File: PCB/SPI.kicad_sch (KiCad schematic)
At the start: 21 parts, among them J3 Trackpad, J4 OLED_Breakout, J6 SSD1351, U4 PMW3360DM-T2QU

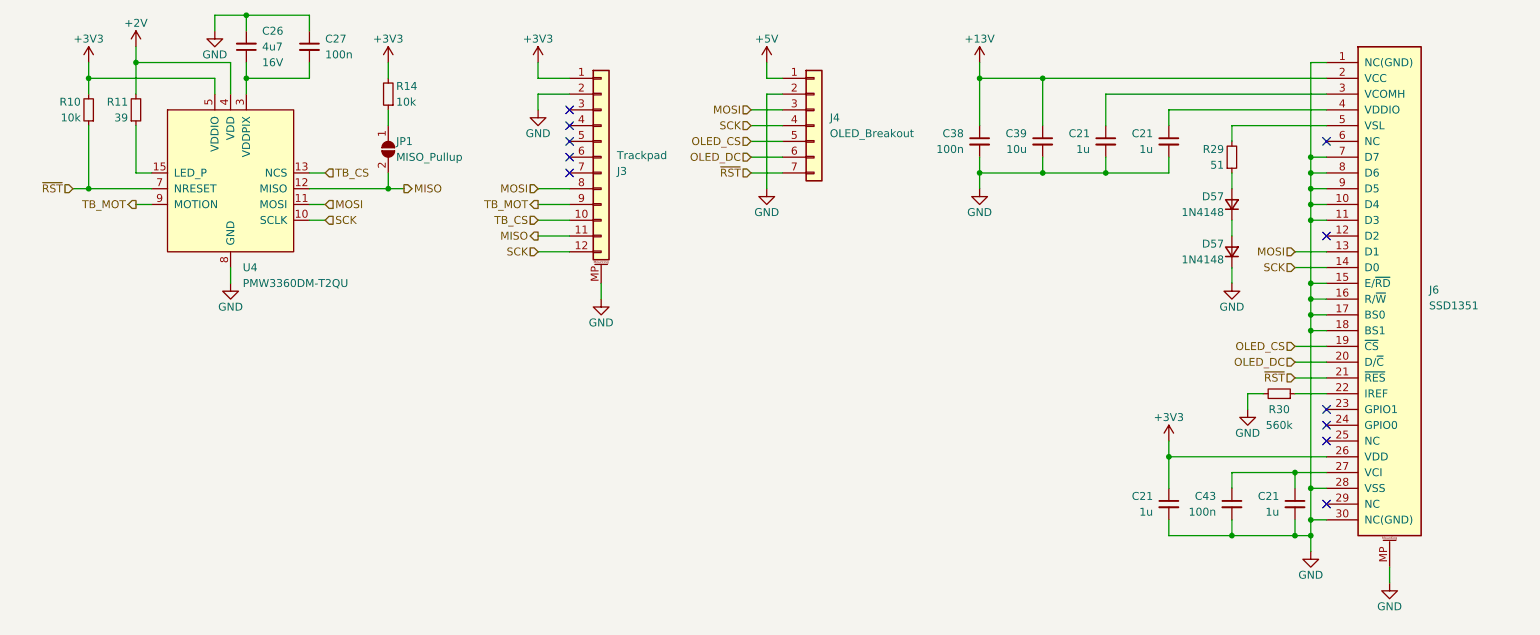
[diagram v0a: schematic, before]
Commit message: 3/4-done update.
Added current and voltage measurement for VBUS in and current measurement for the RGB output. Added PMOS power switch to fully turn off RGB LEDs when not in use. Rerouted the PCB. Moved OLED ribbon cable cutout and expanded it length-wise. Changed position of various components for better routing. Changed bulk capacitance of RGB LEDs to 5 x 22u capacitors. Changed the four N mosfets to two much smaller dual N mosfets. Still need to do RGB routing!
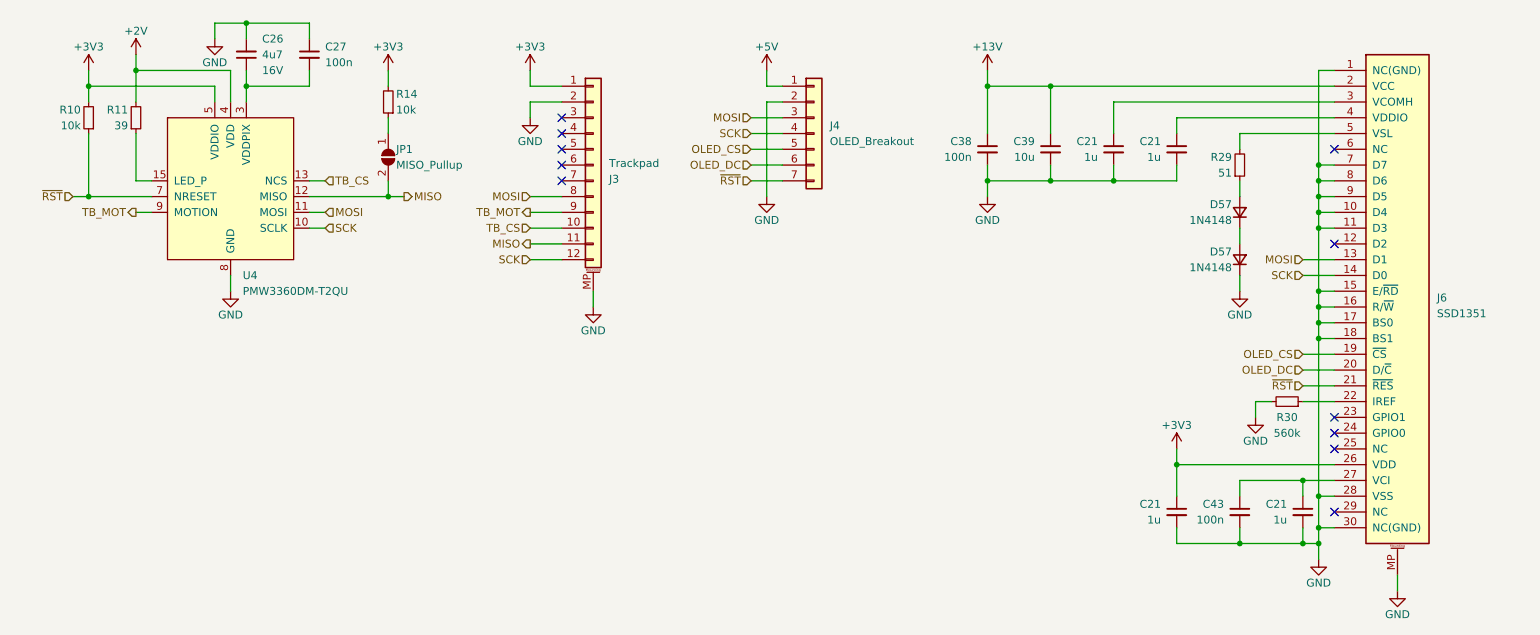
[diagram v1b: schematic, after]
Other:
- moved on the sheet: C21, C26, C27, C38, C39, C43, D57, J3, J4, J6, JP1, R10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

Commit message: 05/05/2023 update.
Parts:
- removed D57 (x2): 1N4148, Honeydew:D_SOD-323, symbol Device:D_Small
- removed JP1: MISO_Pullup, Jumper:SolderJumper-2_P1.3mm_Open_Pad1.0x1.5mm, symbol Jumper:SolderJumper_2_Open
- added D57 (x2): 1N4148, Honeydew:D_SOD-323, symbol Device:D_Small
- added JP2: MISO Pullup, Honeydew:SolderJumper-2_P1.2mm_Open_Pad1.0x1.0mm, symbol Honeydew:SolderJumper_2_Open
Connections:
- net GND: now also D57.1 (K)
- net MISO: now also JP2.2 (B)
- net at R14.1: now also JP2.1 (A)
- net at R29.1: now also D57.2 (A)
- new net: D57.1 (K), D57.2 (A)
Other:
- moved on the sheet: R14

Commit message: Updated BOM. Added new tentative plate file.
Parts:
- U4: now in the parts list
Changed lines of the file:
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@@
   )
   (symbol (lib_name "PMW3360DM-T2QU_1") (lib_id "Ogen:PMW3360DM-T2QU") (at 45.72 43.18 0) (unit 1)
-    (in_bom no) (on_board yes) (dnp no) (fields_autoplaced)
+    (in_bom yes) (on_board yes) (dnp no) (fields_autoplaced)
     (property "Reference" "U4" (at 47.6759 58.42 0)
       (effects (font (size 1.27 1.27)) (justify left))

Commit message: Initial V2.1 update.
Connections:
- net ~{RST}: no longer J4.7 (Pin_7), J6.21 (~{RES})
- new net OLED_~{RST}: J4.7 (Pin_7), J6.21 (~{RES})
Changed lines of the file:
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@@
   (title_block
     (title "Honeydew unified split ergonomic keyboard")
-    (date "2023-04-08")
-    (rev "V2.0")
+    (date "2023-06-27")
+    (rev "V2.1")
     (company "Created by Ariamelon (https://github.com/Ariamelon/Honeydew/)")
     (comment 1 "All capacitors 50V unless otherwise specified.")
@@
     (effects (font (size 1.27 1.27)) (justify right))
   )
+  (hierarchical_label "OLED_~{RST}" (shape input) (at 218.44 76.2 180) (fields_autoplaced)
+    (effects (font (size 1.27 1.27)) (justify right))
+  )
   (hierarchical_label "MOSI" (shape input) (at 60.96 48.26 0) (fields_autoplaced)
     (effects (font (size 1.27 1.27)) (justify left))
   )
+  (hierarchical_label "OLED_~{RST}" (shape input) (at 129.54 43.18 180) (fields_autoplaced)
+    (effects (font (size 1.27 1.27)) (justify right))
+  )
   (hierarchical_label "MOSI" (shape input) (at 218.44 55.88 180) (fields_autoplaced)
     (effects (font (size 1.27 1.27)) (justify right))
@@
     (effects (font (size 1.27 1.27)) (justify right))
   )
-  (hierarchical_label "~{RST}" (shape input) (at 129.54 43.18 180) (fields_autoplaced)
-    (effects (font (size 1.27 1.27)) (justify right))
-  )
   (hierarchical_label "SCK" (shape input) (at 129.54 35.56 180) (fields_autoplaced)
     (effects (font (size 1.27 1.27)) (justify right))
   )
-  (hierarchical_label "~{RST}" (shape input) (at 218.44 76.2 180) (fields_autoplaced)
-    (effects (font (size 1.27 1.27)) (justify right))
-  )

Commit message: In progress update
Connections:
- net ~{RST} renamed TB_~{RST}
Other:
- moved on the sheet: C21, C26, C27, C38, C39, C43, D57, J3, J4, J6, JP2, R10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
